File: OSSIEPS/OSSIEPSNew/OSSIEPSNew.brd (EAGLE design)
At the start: 94 x 88 mm, 100 parts, among them U1 MAX890L, U10 LTC4411, U2 MAX890L, U3 LTC4411, U4 LTC4425, U5 SN74LVC1T45-EP, U6 LT3479, U7 LTC4411, U8 LT3652, U9 MAX4376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

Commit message: all values for tuned results are updated
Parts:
- added R41, R42: 1M, OSSI:R0603(1608)
- C1: value (none) -> 100nF
- C11: value (none) -> 22nF
- C2, C3: value 100nF, 0805 -> 1uF, 0805
- C22: value 1uF, 100V -> 1uF, 100V, 1206
- D4, D5: value PMEG6020EP -> PMEG3050BEP
- R11, R2, R6: value 47k -> 100k
- R35: value 20m / 10m -> 10m
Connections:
- net ANT_COIL1: now also R41.2
- net ANT_COIL2: now also R42.2
- net GND: now also R41.1, R42.1

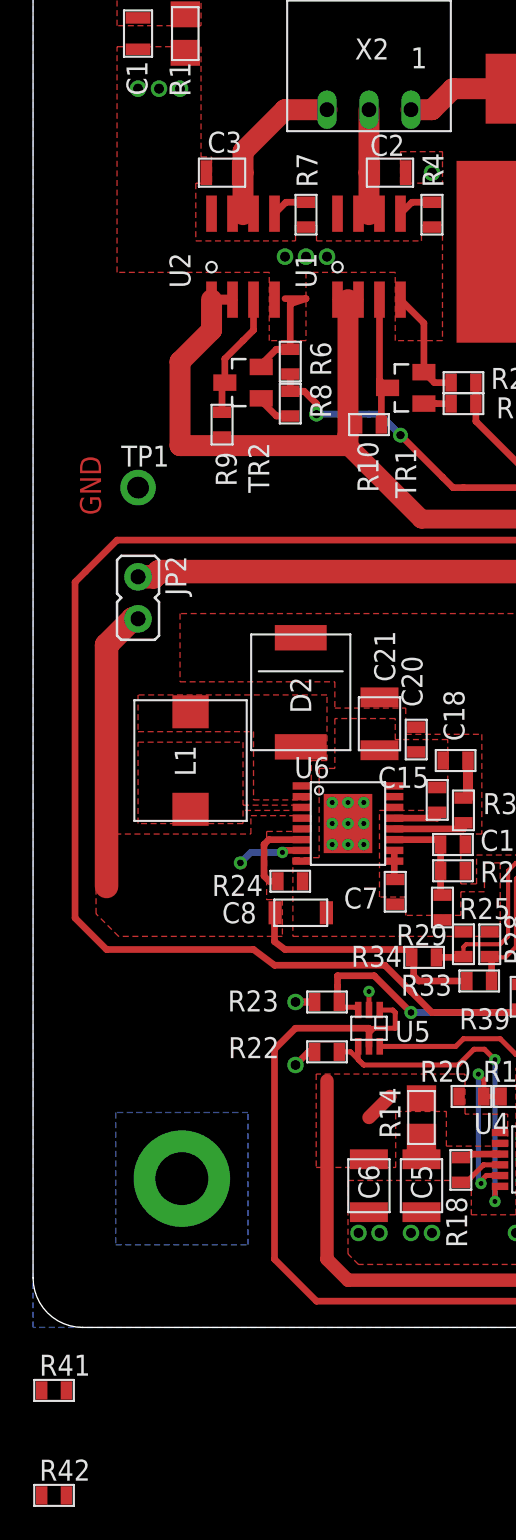
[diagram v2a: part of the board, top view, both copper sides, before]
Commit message: design flies are added
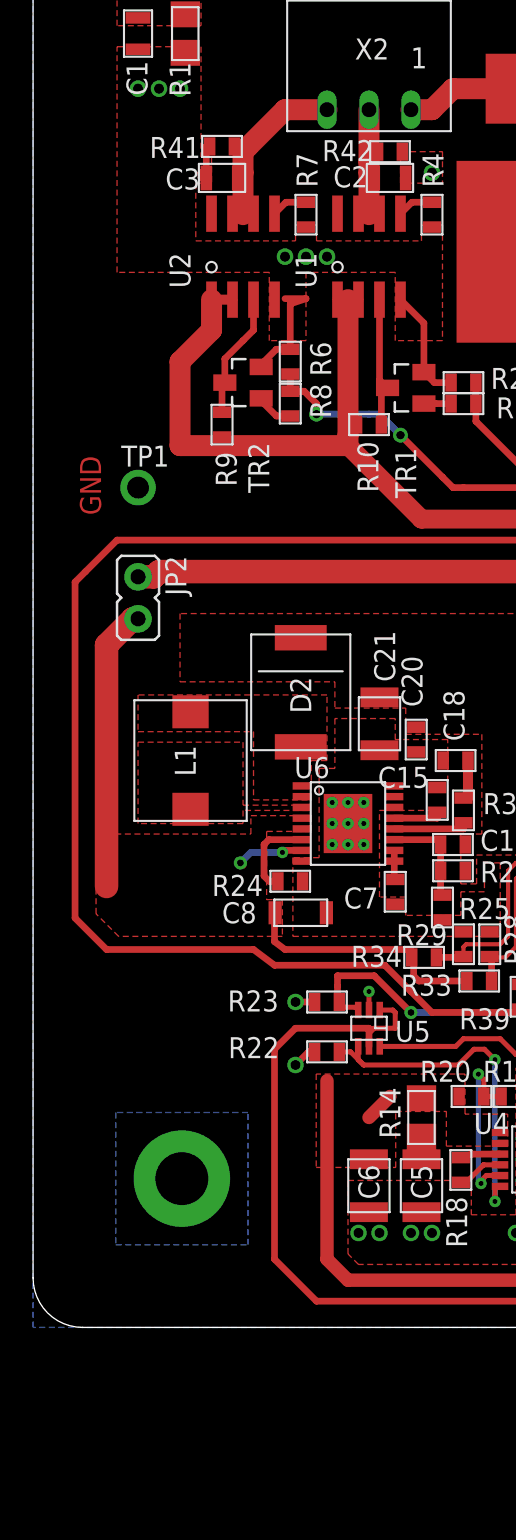
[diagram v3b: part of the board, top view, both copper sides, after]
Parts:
- moved R42 83.8 mm to (21.6, 71.1), turned to 180 degrees
- moved R41 75.9 mm to (11.4, 71.4)
- moved C2 0.32 mm to (21.6, 69.5)
- moved C3 0.32 mm to (11.4, 69.5)
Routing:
- net GND: track 40.1 -> 41.7 mm
- net ANT_COIL2: track 7.99 -> 9.28 mm
- net ANT_COIL1: track 12.0 -> 13.2 mm
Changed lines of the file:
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@@
 <?xml version="1.0" encoding="utf-8"?>
 <!DOCTYPE eagle SYSTEM "eagle.dtd">
-<eagle version="6.1">
+<eagle version="6.5.0">
 <drawing>
 <settings>
@@
 <layer number="16" name="Bottom" color="1" fill="1" visible="yes" active="yes"/>
 <layer number="17" name="Pads" color="2" fill="1" visible="yes" active="yes"/>
-<layer number="18" name="Vias" color="2" fill="1" visible="yes" active="yes"/>
+<layer number="18" name="Vias" color="2" fill="1" visible="no" active="yes"/>
 <layer number="19" name="Unrouted" color="6" fill="1" visible="yes" active="yes"/>
 <layer number="20" name="Dimension" color="15" fill="1" visible="yes" active="yes"/>
@@
 </class>
 </classes>
-<designrules>
+<designrules name="default">
 <description language="de">&lt;b&gt;EAGLE Design Rules&lt;/b&gt;
 &lt;p&gt;
@@
 <attribute name="VALUE" x="15.875" y="55.245" size="1.27" layer="27" rot="R90"/>
 </element>
-<element name="C3" library="OSSI" package="C0805(2012)" value="1uF, 0805" x="11.43" y="69.85" smashed="yes" rot="R180">
-<attribute name="NAME" x="12.6365" y="72.3265" size="1.27" layer="25" font="vector" rot="R180"/>
-<attribute name="VALUE" x="12.319" y="72.136" size="1.27" layer="27" rot="R180"/>
-</element>
-<element name="C2" library="OSSI" package="C0805(2012)" value="1uF, 0805" x="21.59" y="69.85" smashed="yes">
-<attribute name="NAME" x="20.3835" y="70.866" size="1.27" layer="25" font="vector"/>
-<attribute name="VALUE" x="20.701" y="67.564" size="1.27" layer="27"/>
+<element name="C3" library="OSSI" package="C0805(2012)" value="1uF, 0805" x="11.43" y="69.5325" smashed="yes" rot="R180">
+<attribute name="NAME" x="10.0965" y="70.104" size="1.27" layer="25" font="vector" rot="R180"/>
+<attribute name="VALUE" x="12.319" y="71.8185" size="1.27" layer="27" rot="R180"/>
+</element>
+<element name="C2" library="OSSI" package="C0805(2012)" value="1uF, 0805" x="21.59" y="69.5325" smashed="yes">
+<attribute name="NAME" x="18.161" y="68.961" size="1.27" layer="25" font="vector"/>
+<attribute name="VALUE" x="20.701" y="67.2465" size="1.27" layer="27"/>
 </element>
 <element name="D4" library="OSSI" package="PMEG6020EP" value="PMEG3050BEP" x="64.77" y="36.83" smashed="yes" rot="R90">
@@
 <attribute name="VALUE" x="15.34" y="80.8425" size="1.27" layer="27"/>
 </element>
-<element name="R41" library="OSSI" package="R0603(1608)" value="1M" x="1.27" y="-3.81"/>
-<element name="R42" library="OSSI" package="R0603(1608)" value="1M" x="1.27" y="-10.16"/>
+<element name="R41" library="OSSI" package="R0603(1608)" value="1M" x="11.43" y="71.4375" smashed="yes">
+<attribute name="NAME" x="7.0485" y="70.739" size="1.27" layer="25" font="vector"/>
+<attribute name="VALUE" x="10.541" y="69.4055" size="1.27" layer="27"/>
+</element>
+<element name="R42" library="OSSI" package="R0603(1608)" value="1M" x="21.59" y="71.12" smashed="yes" rot="R180">
+<attribute name="NAME" x="20.574" y="71.8185" size="1.27" layer="25" font="vector" rot="R180"/>
+<attribute name="VALUE" x="22.479" y="73.152" size="1.27" layer="27" rot="R180"/>
+</element>
 </elements>
 <signals>
@@
 <wire x1="41.5925" y1="10.68" x2="43.35" y2="10.68" width="0.4064" layer="1"/>
 <wire x1="43.35" y1="10.68" x2="43.35" y2="10.48" width="0.4064" layer="1"/>
-<wire x1="17.03" y1="16.66875" x2="16.98625" y2="16.66875" width="0.4064" layer="1"/>
 <via x="61.595" y="59.69" extent="1-16" drill="0.6"/>
 <wire x1="63.5" y1="60.44" x2="62.0275" y2="60.44" width="0.4064" layer="1"/>
@@
 <via x="15.875" y="15.875" extent="1-16" drill="0.6"/>
 <wire x1="17.03" y1="19.685" x2="15.875" y2="19.685" width="0.4064" layer="1"/>
-<wire x1="17.03" y1="19.685" x2="15.875" y2="19.685" width="0.4064" layer="1"/>
-<wire x1="16.98625" y1="16.66875" x2="16.66875" y2="16.66875" width="0.4064" layer="1"/>
+<wire x1="17.03" y1="16.66875" x2="16.66875" y2="16.66875" width="0.4064" layer="1"/>
 <wire x1="16.66875" y1="16.66875" x2="15.875" y2="15.875" width="0.4064" layer="1"/>
 <via x="20.32" y="20.32" extent="1-16" drill="0.3"/>
@@
 <contactref element="R42" pad="1"/>
 <contactref element="R41" pad="1"/>
-<wire x1="0.52" y1="-3.81" x2="0.52" y2="-10.16" width="0" layer="19" extent="1-1"/>
-<wire x1="19.685" y1="5.715" x2="0.52" y2="-3.81" width="0" layer="19" extent="1-1"/>
+<wire x1="10.68" y1="71.4375" x2="10.4775" y2="71.4375" width="0.4064" layer="1"/>
+<wire x1="10.4775" y1="71.4375" x2="10.4775" y2="69.85" width="0.4064" layer="1"/>
+<wire x1="10.48" y1="69.5325" x2="10.16" y2="69.5325" width="0.4064" layer="1"/>
+<wire x1="10.16" y1="69.5325" x2="10.16" y2="69.85" width="0.4064" layer="1"/>
+<wire x1="10.16" y1="69.85" x2="10.4775" y2="69.85" width="0.4064" layer="1"/>
 </signal>
 <signal name="N$10">
@@
 <wire x1="13.335" y1="67.37" x2="12.76" y2="67.37" width="0.3048" layer="1"/>
 <wire x1="12.76" y1="67.37" x2="12.7" y2="67.31" width="0.3048" layer="1"/>
-<wire x1="12.38" y1="69.85" x2="12.3825" y2="70.1675" width="0.3048" layer="1"/>
+<wire x1="12.38" y1="69.5325" x2="12.3825" y2="70.1675" width="0.3048" layer="1"/>
 <wire x1="12.3825" y1="70.1675" x2="12.7" y2="69.85" width="0.3048" layer="1"/>
 <contactref element="X2" pad="3"/>
 <wire x1="12.7" y1="69.85" x2="12.7" y2="71.12" width="1.27" layer="1"/>
-<wire x1="12.7" y1="71.12" x2="15.24" y2="73.66" width="1.27" layer="1"/>
+<wire x1="12.7" y1="71.12" x2="13.0175" y2="71.4375" width="1.27" layer="1"/>
+<wire x1="13.0175" y1="71.4375" x2="15.24" y2="73.66" width="1.27" layer="1"/>
 <wire x1="15.24" y1="73.66" x2="17.78" y2="73.66" width="1.27" layer="1"/>
 <contactref element="R41" pad="2"/>
-<wire x1="2.02" y1="-3.81" x2="12.065" y2="67.37" width="0" layer="19" extent="1-1"/>
+<wire x1="12.18" y1="71.4375" x2="13.0175" y2="71.4375" width="0.4064" layer="1"/>
 </signal>
 <signal name="ANT_COIL2">
@@
 <wire x1="20.895" y1="67.31" x2="20.955" y2="67.37" width="0.3048" layer="1"/>
 <contactref element="X2" pad="2"/>
-<wire x1="20.32" y1="69.85" x2="20.32" y2="73.66" width="1.27" layer="1"/>
-<wire x1="20.64" y1="69.85" x2="20.32" y2="69.85" width="0.3048" layer="1"/>
+<wire x1="20.32" y1="69.85" x2="20.32" y2="70.485" width="1.27" layer="1"/>
+<wire x1="20.32" y1="70.485" x2="20.32" y2="73.66" width="1.27" layer="1"/>
+<wire x1="20.64" y1="69.5325" x2="20.32" y2="69.85" width="0.3048" layer="1"/>
 <contactref element="R42" pad="2"/>
-<wire x1="2.02" y1="-10.16" x2="19.685" y2="67.37" width="0" layer="19" extent="1-1"/>
+<wire x1="20.84" y1="71.12" x2="20.32" y2="71.12" width="0.4064" layer="1"/>
+<wire x1="20.32" y1="71.12" x2="20.32" y2="70.485" width="0.4064" layer="1"/>
 </signal>
 <signal name="VBAT">
